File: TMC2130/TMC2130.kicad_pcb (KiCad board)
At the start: 8 copper layers, 15.2 x 20.5 mm, 23 parts, among them J1 DIAG, Q1 BCX56, U1 TMC2130-TA

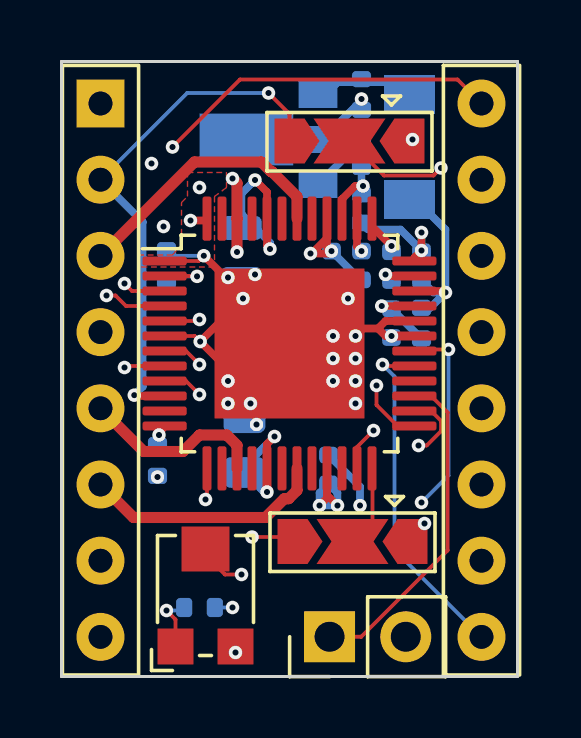
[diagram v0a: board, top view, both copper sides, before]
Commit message: changed to 6L
deleted 2 ground pours to allow for 8L assembly on JLCPCB
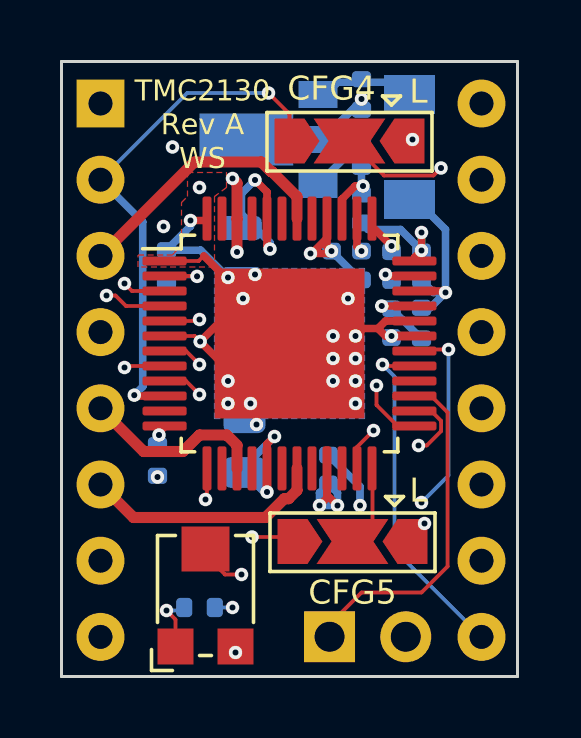
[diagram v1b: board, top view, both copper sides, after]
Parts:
- C3: value 470nF/16V -> 220nF/16V
- C4: value 22nF/63V -> 22nF/50V
- D1: value D_Zener -> 5.6V
- R5: value 2.2R -> 1R
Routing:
- net GND: track 22.2 -> 24.6 mm, vias 29 -> 27
- net +5V: track 20.2 -> 21.0 mm
- net /DIAG1: track 11.1 -> 11.6 mm
- added copper zone on In1.Cu, net /1A
- added copper zone on B.Cu, net GND
- added copper zone on In1.Cu, net Vdrive
- removed copper zone on In6.Cu, net /1A
- removed copper zone on In1.Cu, net GND
- removed copper zone on In5.Cu, net GND
- removed copper zone on In6.Cu, net Vdrive
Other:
- copper layers 8 -> 6
- board text added: "CFG4"
- board text added: "CFG5"
- board text added: "L"
- board text added: "TMC2130 Rev A WS"
